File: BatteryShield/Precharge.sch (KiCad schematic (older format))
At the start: 6 parts

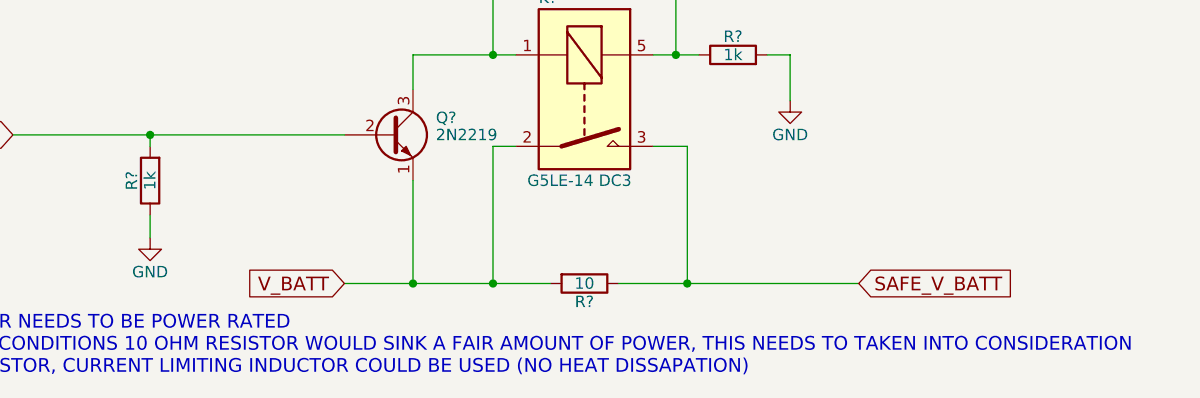
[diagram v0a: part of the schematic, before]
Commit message: Added two pages, cleaned up net names
Cleaned up net names. Added protection/grounding and BBB interface socket. Additional work needs to be done with grounding/mounting holes and 37V rail reverse current protection.
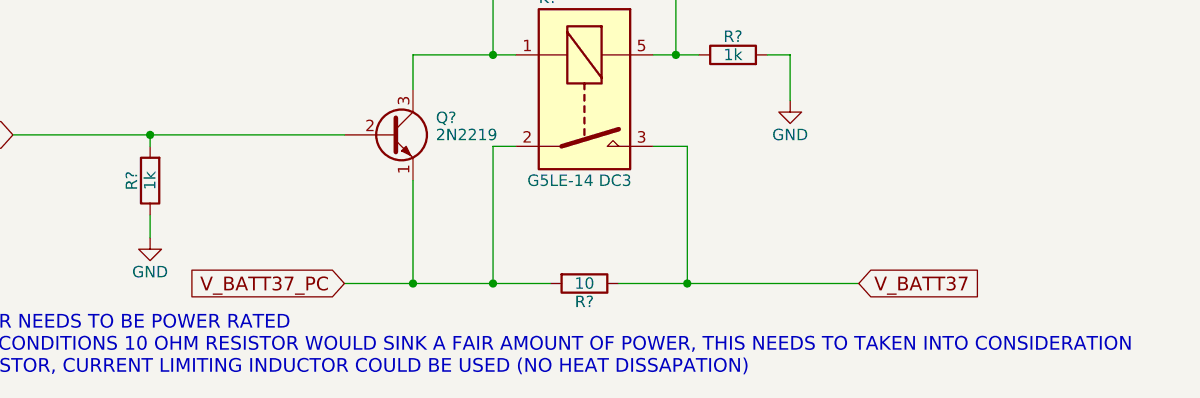
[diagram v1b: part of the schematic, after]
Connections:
- net SAFE_V_BATT renamed V_BATT37
- net V_BATT renamed V_BATT37_PC
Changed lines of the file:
@@
 $Descr A4 11693 8268
 encoding utf-8
-Sheet 4 10
+Sheet 4 12
 Title ""
 Date ""
@@
 $EndDescr
 Text GLabel 3850 4100 0    60   Input ~ 0
-V_BATT
+V_BATT37_PC
 $Comp
 L R R?
@@
 $EndComp
 Text GLabel 6100 4100 2    60   Input ~ 0
-SAFE_V_BATT
+V_BATT37
 $Comp
 L 2N2219 Q?
@@
 	5300 2500 5300 3100
 Connection ~ 5300 3100
-Text Notes 1600 4600 0    60   ~ 0
-NOTES:\n-10 OHM RESISTOR NEEDS TO BE POWER RATED\n-UNDER VACCUM CONDITIONS 10 OHM RESISTOR WOULD SINK A FAIR AMOUNT OF POWER, THIS NEEDS TO TAKEN INTO CONSIDERATION\n-INSTEAD OF RESISTOR, CURRENT LIMITING INDUCTOR COULD BE USED (NO HEAT DISSAPATION)\n\n
 $Comp
 L R R?
@@
 Wire Wire Line
 	5700 3100 5800 3100
+Text Notes 1600 4600 0    60   ~ 0
+NOTES:\n-10 OHM RESISTOR NEEDS TO BE POWER RATED\n-UNDER VACCUM CONDITIONS 10 OHM RESISTOR WOULD SINK A FAIR AMOUNT OF POWER, THIS NEEDS TO TAKEN INTO CONSIDERATION\n-INSTEAD OF RESISTOR, CURRENT LIMITING INDUCTOR COULD BE USED (NO HEAT DISSAPATION)\n\n
 $EndSCHEMATC

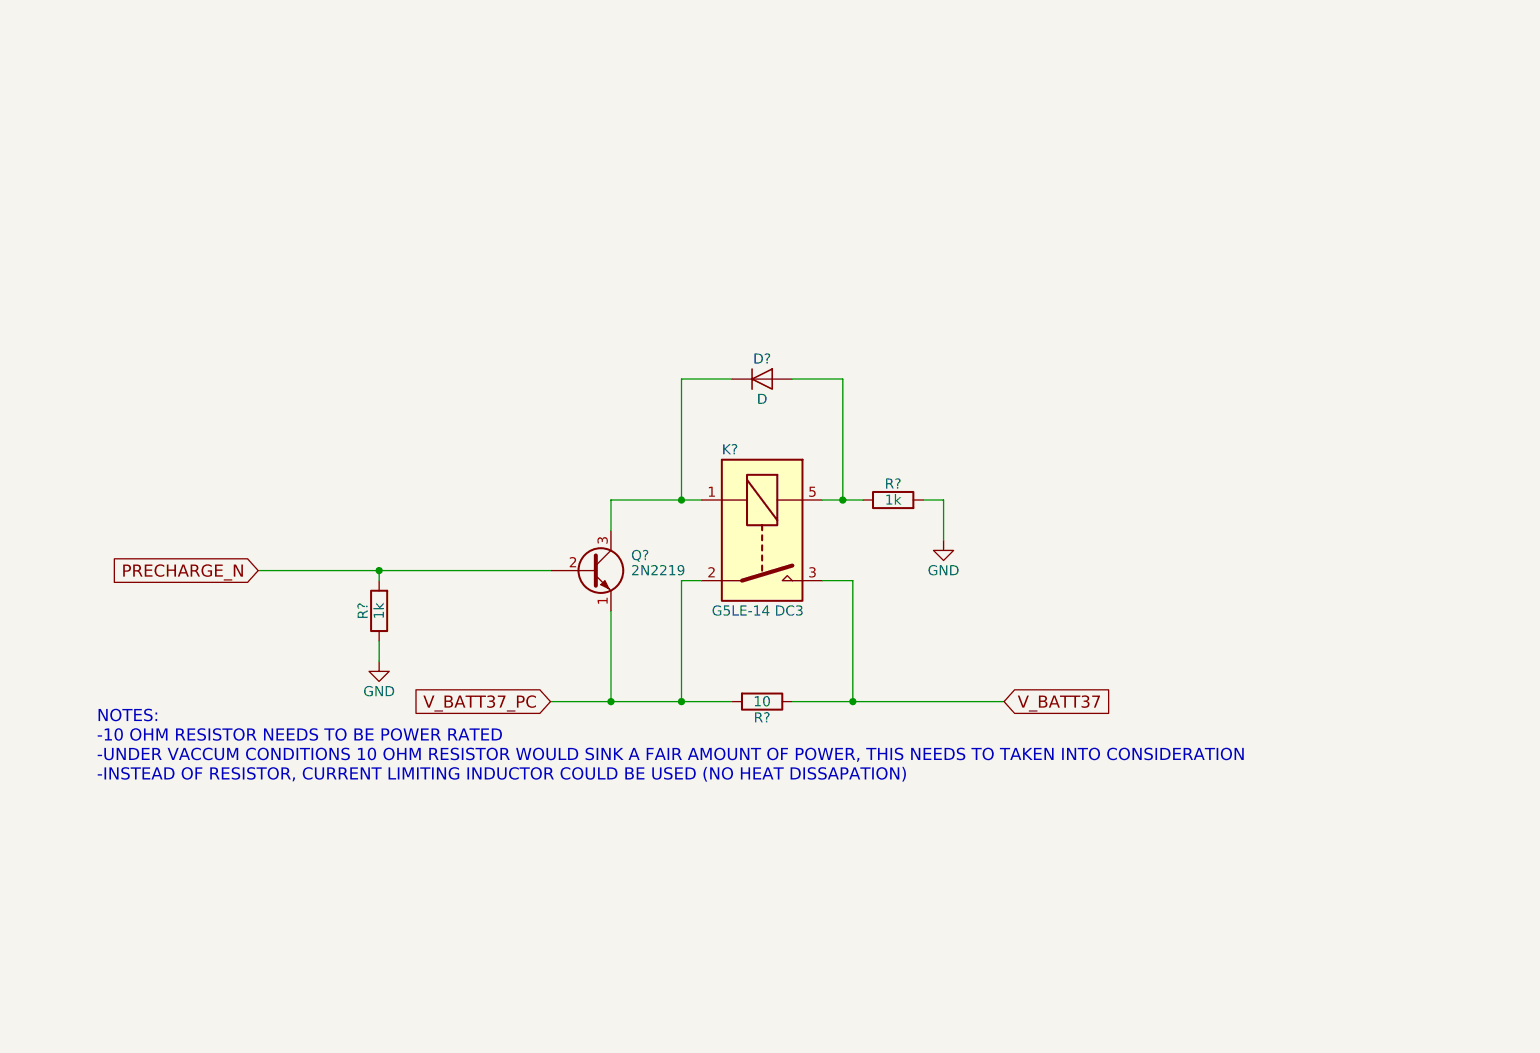
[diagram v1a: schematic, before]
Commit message: Associated a lot of footprints
Now I need to add a lot more :(
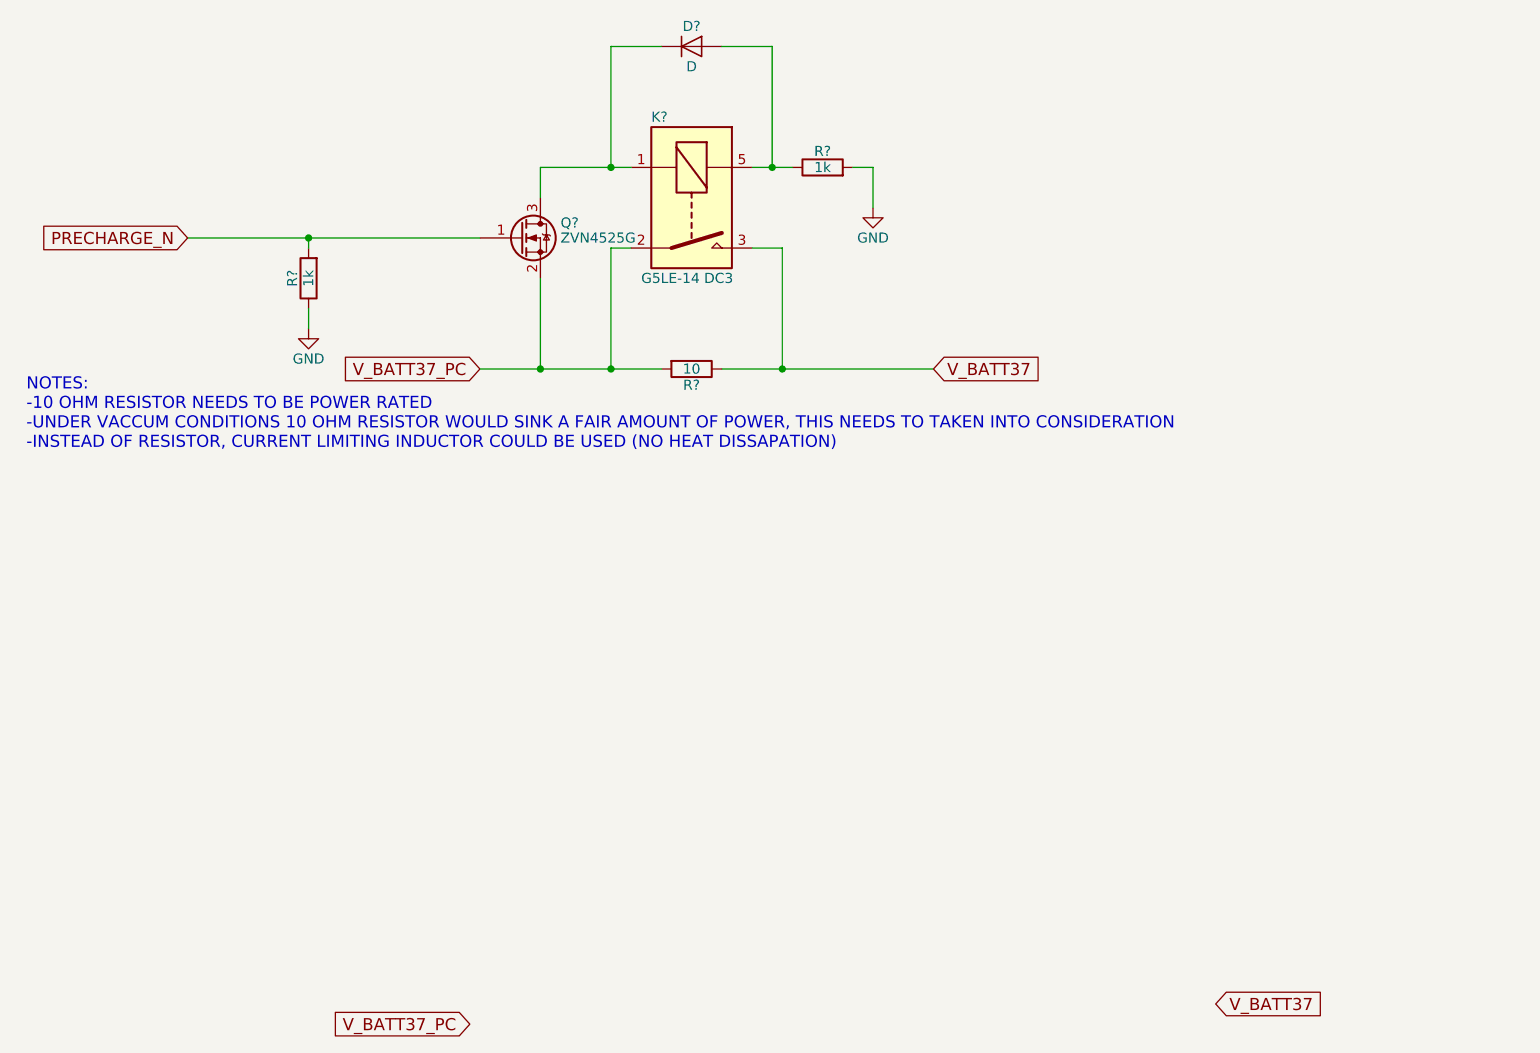
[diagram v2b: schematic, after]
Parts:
- removed Q?: 2N2219, TO_SOT_Packages_THT:TO-39-3, symbol 2N2219
- added Q?: ZVN4525G, TO_SOT_Packages_SMD:SOT-23, symbol BSS138
- R?: footprint (none) -> TO-263-2
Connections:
- net PRECHARGE_N: now also Q?.1 (G)
- net V_BATT37_PC: now also Q?.2 (S)
- net at D?.1 (K), K?.1: now also Q?.3 (D)
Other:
- moved on the sheet: D?, K?, R?
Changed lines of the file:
@@
 Comment4 ""
 $EndDescr
-Text GLabel 3850 4100 0    60   Input ~ 0
+Text GLabel 3500 2450 0    60   Input ~ 0
 V_BATT37_PC
 $Comp
 L R R?
 U 1 1 5B0F060B
-P 4900 4100
-F 0 "R?" V 4980 4100 50  0000 C CNN
-F 1 "10" V 4900 4100 50  0000 C CNN
-F 2 "" V 4830 4100 50  0001 C CNN
-F 3 "" H 4900 4100 50  0001 C CNN
-	1    4900 4100
+P 4550 2450
+F 0 "R?" V 4630 2450 50  0000 C CNN
+F 1 "10" V 4550 2450 50  0000 C CNN
+F 2 "TO-263-2" V 4480 2450 50  0001 C CNN
+F 3 "http://www.caddock.com/Online_catalog/Mrktg_Lit/MP725.pdf" H 4550 2450 50  0001 C CNN
+	1    4550 2450
 	0    1    1    0
 $EndComp
@@
 L G5Q-1A K?
 U 1 1 5B0F0DA1
-P 4700 3100
-F 0 "K?" V 4450 3100 50  0000 L CNN
-F 1 "G5LE-14 DC3" V 5250 3050 50  0000 L CNN
-F 2 "Relays_THT:Relay_SPST-NO_OMRON-G5Q" H 5250 3250 50  0001 L CNN
-F 3 "" H 5800 2800 50  0001 C CNN
-	1    4700 3100
+P 4350 1450
+F 0 "K?" V 4100 1450 50  0000 L CNN
+F 1 "G5LE-14 DC3" V 4900 1400 50  0000 L CNN
+F 2 "Relays_THT:Relay_SPST-NO_OMRON-G5Q" H 4900 1600 50  0001 L CNN
+F 3 "" H 5450 1150 50  0001 C CNN
+	1    4350 1450
 	0    1    1    0
 $EndComp
-Text GLabel 6100 4100 2    60   Input ~ 0
+Text GLabel 5750 2450 2    60   Input ~ 0
 V_BATT37
-$Comp
-L 2N2219 Q?
-U 1 1 5B0F19CB
-P 4050 3450
-F 0 "Q?" H 4250 3525 50  0000 L CNN
-F 1 "2N2219" H 4250 3450 50  0000 L CNN
-F 2 "TO_SOT_Packages_THT:TO-39-3" H 4250 3375 50  0001 L CIN
-F 3 "" H 4050 3450 50  0001 L CNN
-	1    4050 3450
-	1    0    0    -1
-$EndComp
 $Comp
 L GND #PWR?
 U 1 1 5B0F1AA8
-P 5800 3300
-F 0 "#PWR?" H 5800 3050 50  0001 C CNN
-F 1 "GND" H 5800 3150 50  0000 C CNN
-F 2 "" H 5800 3300 50  0001 C CNN
-F 3 "" H 5800 3300 50  0001 C CNN
-	1    5800 3300
+P 5450 1650
+F 0 "#PWR?" H 5450 1400 50  0001 C CNN
+F 1 "GND" H 5450 1500 50  0000 C CNN
+F 2 "" H 5450 1650 50  0001 C CNN
+F 3 "" H 5450 1650 50  0001 C CNN
+	1    5450 1650
 	1    0    0    -1
 $EndComp
-Text GLabel 2400 3450 0    60   Input ~ 0
+Text GLabel 2050 1800 0    60   Input ~ 0
 PRECHARGE_N
 $Comp
 L GND #PWR?
 U 1 1 5B0F1D11
-P 3000 3900
-F 0 "#PWR?" H 3000 3650 50  0001 C CNN
-F 1 "GND" H 3000 3750 50  0000 C CNN
-F 2 "" H 3000 3900 50  0001 C CNN
-F 3 "" H 3000 3900 50  0001 C CNN
-	1    3000 3900
+P 2650 2250
+F 0 "#PWR?" H 2650 2000 50  0001 C CNN
+F 1 "GND" H 2650 2100 50  0000 C CNN
+F 2 "" H 2650 2250 50  0001 C CNN
+F 3 "" H 2650 2250 50  0001 C CNN
+	1    2650 2250
 	1    0    0    -1
 $EndComp
@@
 L R R?
 U 1 1 5B0F1D2F
-P 3000 3650
-F 0 "R?" V 3080 3650 50  0000 C CNN
-F 1 "1k" V 3000 3650 50  0000 C CNN
-F 2 "" V 2930 3650 50  0001 C CNN
-F 3 "" H 3000 3650 50  0001 C CNN
-	1    3000 3650
+P 2650 2000
+F 0 "R?" V 2730 2000 50  0000 C CNN
+F 1 "1k" V 2650 2000 50  0000 C CNN
+F 2 "" V 2580 2000 50  0001 C CNN
+F 3 "" H 2650 2000 50  0001 C CNN
+	1    2650 2000
 	-1   0    0    1
 $EndComp
@@
 L D D?
 U 1 1 5B0F22D2
-P 4900 2500
-F 0 "D?" H 4900 2600 50  0000 C CNN
-F 1 "D" H 4900 2400 50  0000 C CNN
-F 2 "" H 4900 2500 50  0001 C CNN
-F 3 "" H 4900 2500 50  0001 C CNN
-	1    4900 2500
+P 4550 850
+F 0 "D?" H 4550 950 50  0000 C CNN
+F 1 "D" H 4550 750 50  0000 C CNN
+F 2 "" H 4550 850 50  0001 C CNN
+F 3 "" H 4550 850 50  0001 C CNN
+	1    4550 850
 	1    0    0    -1
 $EndComp
 Wire Wire Line
-	3850 4100 4750 4100
+	3500 2450 4400 2450
 Wire Wire Line
-	5050 4100 6100 4100
+	4700 2450 5750 2450
 Wire Wire Line
-	4500 4100 4500 3500
+	4150 2450 4150 1850
 Wire Wire Line
-	4500 3500 4600 3500
-Connection ~ 4500 4100
+	4150 1850 4250 1850
+Connection ~ 4150 2450
 Wire Wire Line
-	5200 3500 5350 3500
+	4850 1850 5000 1850
 Wire Wire Line
-	5350 3500 5350 4100
-Connection ~ 5350 4100
+	5000 1850 5000 2450
+Connection ~ 5000 2450
 Wire Wire Line
-	4150 4100 4150 3650
-Connection ~ 4150 4100
+	3800 2450 3800 2000
+Connection ~ 3800 2450
 Wire Wire Line
-	4150 3250 4150 3100
+	3800 1600 3800 1450
 Wire Wire Line
-	4150 3100 4600 3100
+	3800 1450 4250 1450
 Wire Wire Line
-	5800 3100 5800 3300
+	5450 1450 5450 1650
 Wire Wire Line
-	2400 3450 3850 3450
+	2050 1800 3500 1800
 Wire Wire Line
-	3000 3500 3000 3450
-Connection ~ 3000 3450
+	2650 1850 2650 1800
+Connection ~ 2650 1800
 Wire Wire Line
-	3000 3800 3000 3900
+	2650 2150 2650 2250
 Wire Wire Line
-	4500 3100 4500 2500
+	4150 1450 4150 850
 Wire Wire Line
-	4500 2500 4750 2500
-Connection ~ 4500 3100
+	4150 850  4400 850
+Connection ~ 4150 1450
 Wire Wire Line
-	5050 2500 5300 2500
+	4700 850  4950 850
 Wire Wire Line
-	5300 2500 5300 3100
-Connection ~ 5300 3100
+	4950 850  4950 1450
+Connection ~ 4950 1450
 $Comp
 L R R?
 U 1 1 5B103E03
-P 5550 3100
-F 0 "R?" V 5630 3100 50  0000 C CNN
-F 1 "1k" V 5550 3100 50  0000 C CNN
-F 2 "" V 5480 3100 50  0001 C CNN
-F 3 "" H 5550 3100 50  0001 C CNN
-	1    5550 3100
+P 5200 1450
+F 0 "R?" V 5280 1450 50  0000 C CNN
+F 1 "1k" V 5200 1450 50  0000 C CNN
+F 2 "" V 5130 1450 50  0001 C CNN
+F 3 "" H 5200 1450 50  0001 C CNN
+	1    5200 1450
 	0    -1   -1   0
 $EndComp
 Wire Wire Line
-	5200 3100 5400 3100
+	4850 1450 5050 1450
 Wire Wire Line
-	5700 3100 5800 3100
-Text Notes 1600 4600 0    60   ~ 0
+	5350 1450 5450 1450
+Text Notes 1250 2950 0    60   ~ 0
 NOTES:\n-10 OHM RESISTOR NEEDS TO BE POWER RATED\n-UNDER VACCUM CONDITIONS 10 OHM RESISTOR WOULD SINK A FAIR AMOUNT OF POWER, THIS NEEDS TO TAKEN INTO CONSIDERATION\n-INSTEAD OF RESISTOR, CURRENT LIMITING INDUCTOR COULD BE USED (NO HEAT DISSAPATION)\n\n
+Text GLabel 3450 5700 0    60   Input ~ 0
+V_BATT37_PC
+Text GLabel 7150 5600 2    60   Input ~ 0
+V_BATT37
+$Comp
+L BSS138 Q?
+U 1 1 5B298E62
+P 3700 1800
+F 0 "Q?" H 3900 1875 50  0000 L CNN
+F 1 "ZVN4525G" H 3900 1800 50  0000 L CNN
+F 2 "TO_SOT_Packages_SMD:SOT-23" H 3900 1725 50  0001 L CIN
+F 3 "" H 3700 1800 50  0001 L CNN
+	1    3700 1800
+	1    0    0    -1
+$EndComp
 $EndSCHEMATC
